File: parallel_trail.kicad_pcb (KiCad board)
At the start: 2 copper layers, 90 x 45 mm, 90 parts, among them U1 TL074, U3 TL074, U4 DG419LDY, U5 TL072, U6 PT2258

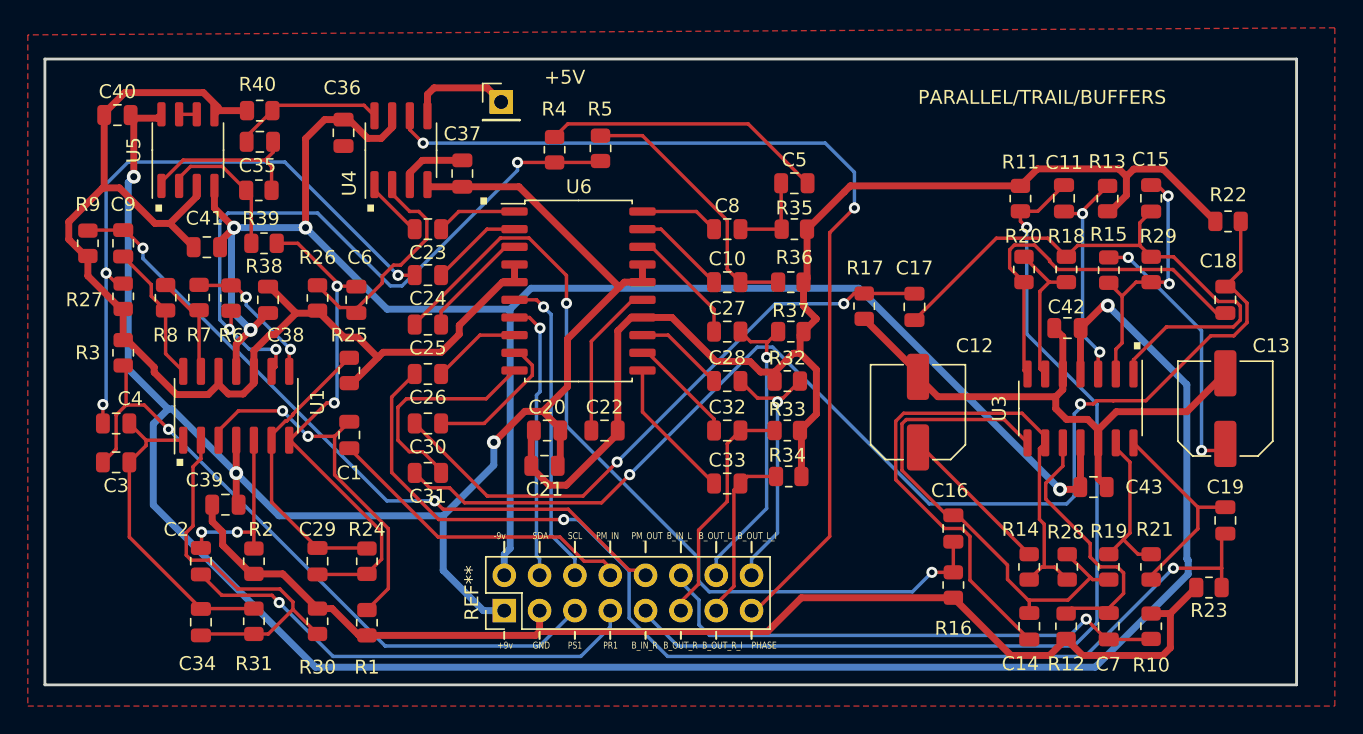
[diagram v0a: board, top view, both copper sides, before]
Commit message: changed dg419 to 3.3V
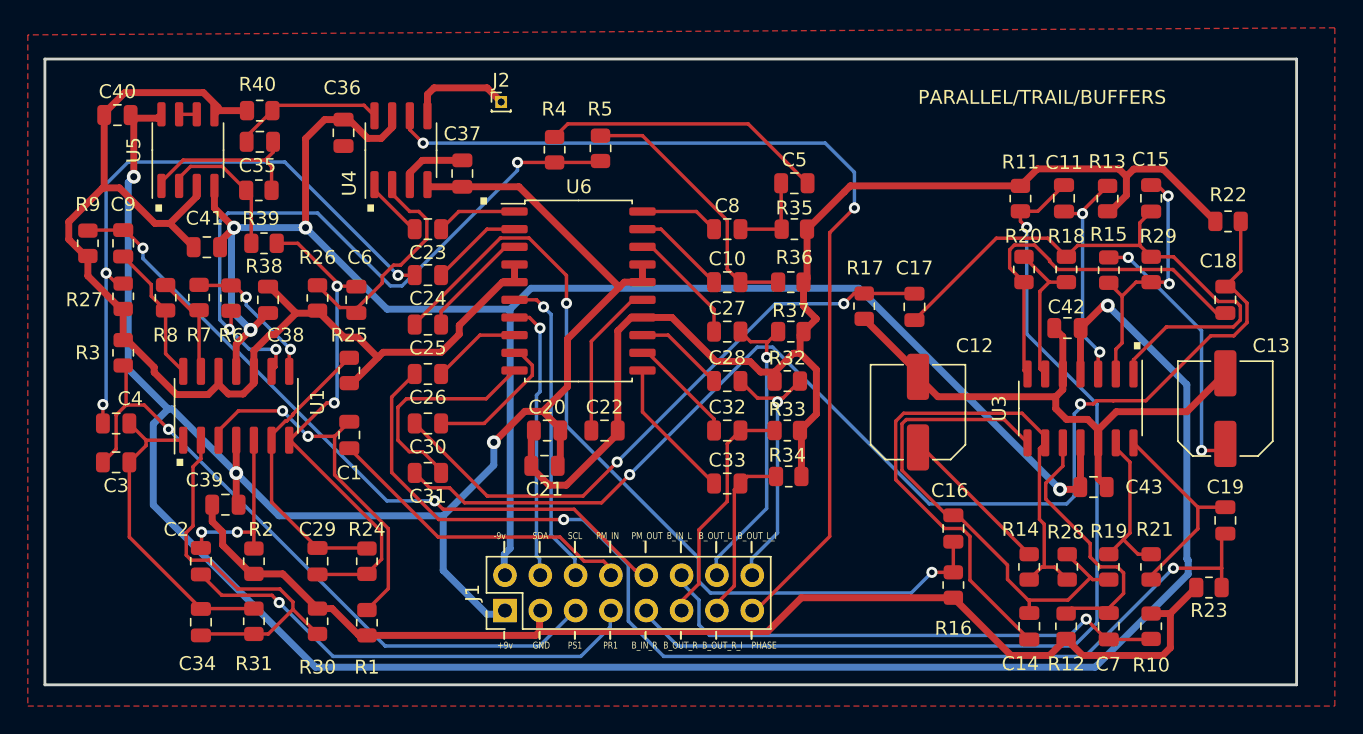
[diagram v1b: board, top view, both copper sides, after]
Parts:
- removed +5V: PinHeader_1x01_P2.54mm_Vertical, Connector_PinHeader_2.54mm:PinHeader_1x01_P2.54mm_Vertical
- removed REF**: PinHeader_2x08_P2.54mm_Vertical, Connector_PinHeader_2.54mm:PinHeader_2x08_P2.54mm_Vertical
- added J1: Conn_01x16_Pin, Connector_PinHeader_2.54mm:PinHeader_2x08_P2.54mm_Vertical, F.Cu at (79.8, 119.1)
- added J2: Conn_01x01_Pin, Connector_PinHeader_1.00mm:PinHeader_1x01_P1.00mm_Vertical, F.Cu at (79.5, 82.5)
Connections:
- U4 pad 5: +5V -> +3.3V
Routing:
- net +5V: track 7.45 -> 0.00 mm
- net +3.3V: track 0.00 -> 7.45 mm

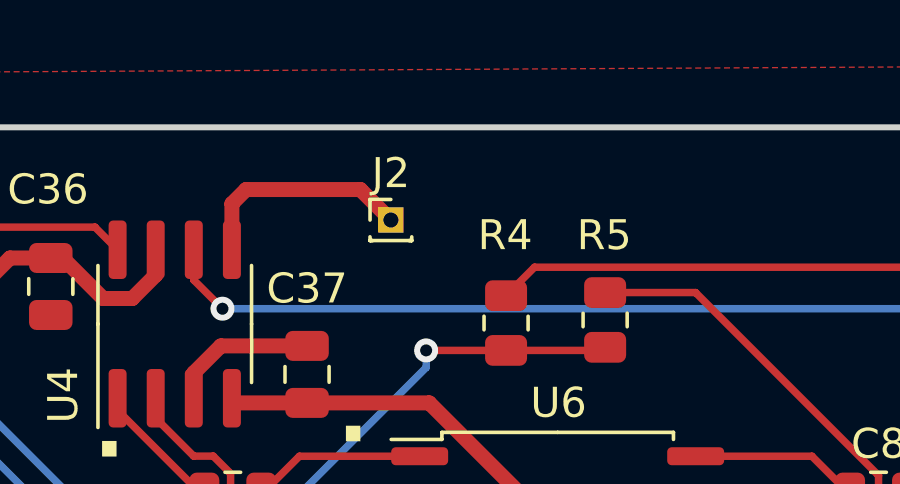
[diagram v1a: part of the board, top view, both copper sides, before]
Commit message: add 3.3v label
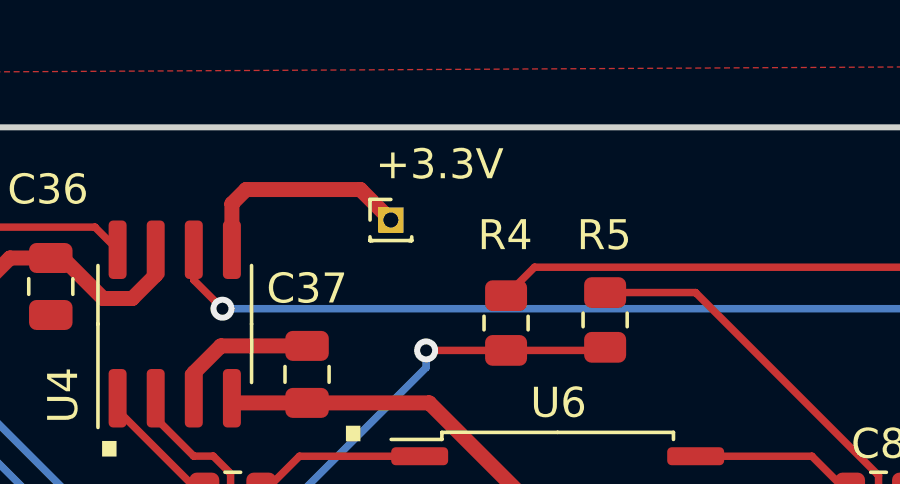
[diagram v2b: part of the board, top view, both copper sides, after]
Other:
- board text added: "+3.3V"
